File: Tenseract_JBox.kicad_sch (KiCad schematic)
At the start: 14 parts, among them J1 MR30PW-M, J10 Conn_01x04_Pin, J11 Conn_01x04_Pin, J12 Conn_01x04_Pin, J15 TEST_IN, J16 TEST_OUT, J17 DO_SEL, J19 DO_SEL, J2 WS2815_01_IN, J3 WS2815_02_IN, J4 MR30PW-FB, J5 WS2815_01_OUT, J6 WS2815_02_OUT, J8 Conn_01x04_Pin

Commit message: Finished 2nd pcb
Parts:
- added J15: DO_SEL2, Connector_PinHeader_2.54mm:PinHeader_1x03_P2.54mm_Vertical, symbol Connector:Conn_01x03_Pin
- J14: renamed from J17; value DO_SEL -> DO_SEL1
- renumbered J12 to J10, J6 to J11, J11 to J12, J16 to J13, J8 to J3, J3 to J4, J10 to J5, J15 to J6, J19 to J7, J4 to J8, J5 to J9
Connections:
- net BO2: now also J15.3 (Pin_3)
- net DO: now also J15.2 (Pin_2)
- net DO1: now also J14.3 (Pin_3); no longer J14.1 (Pin_1)
- net DO2: now also J15.1 (Pin_1); no longer J14.3 (Pin_3)
- net B01 renamed BO1
- net BO1: now also J14.1 (Pin_1)
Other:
- moved on the sheet: J10, J14

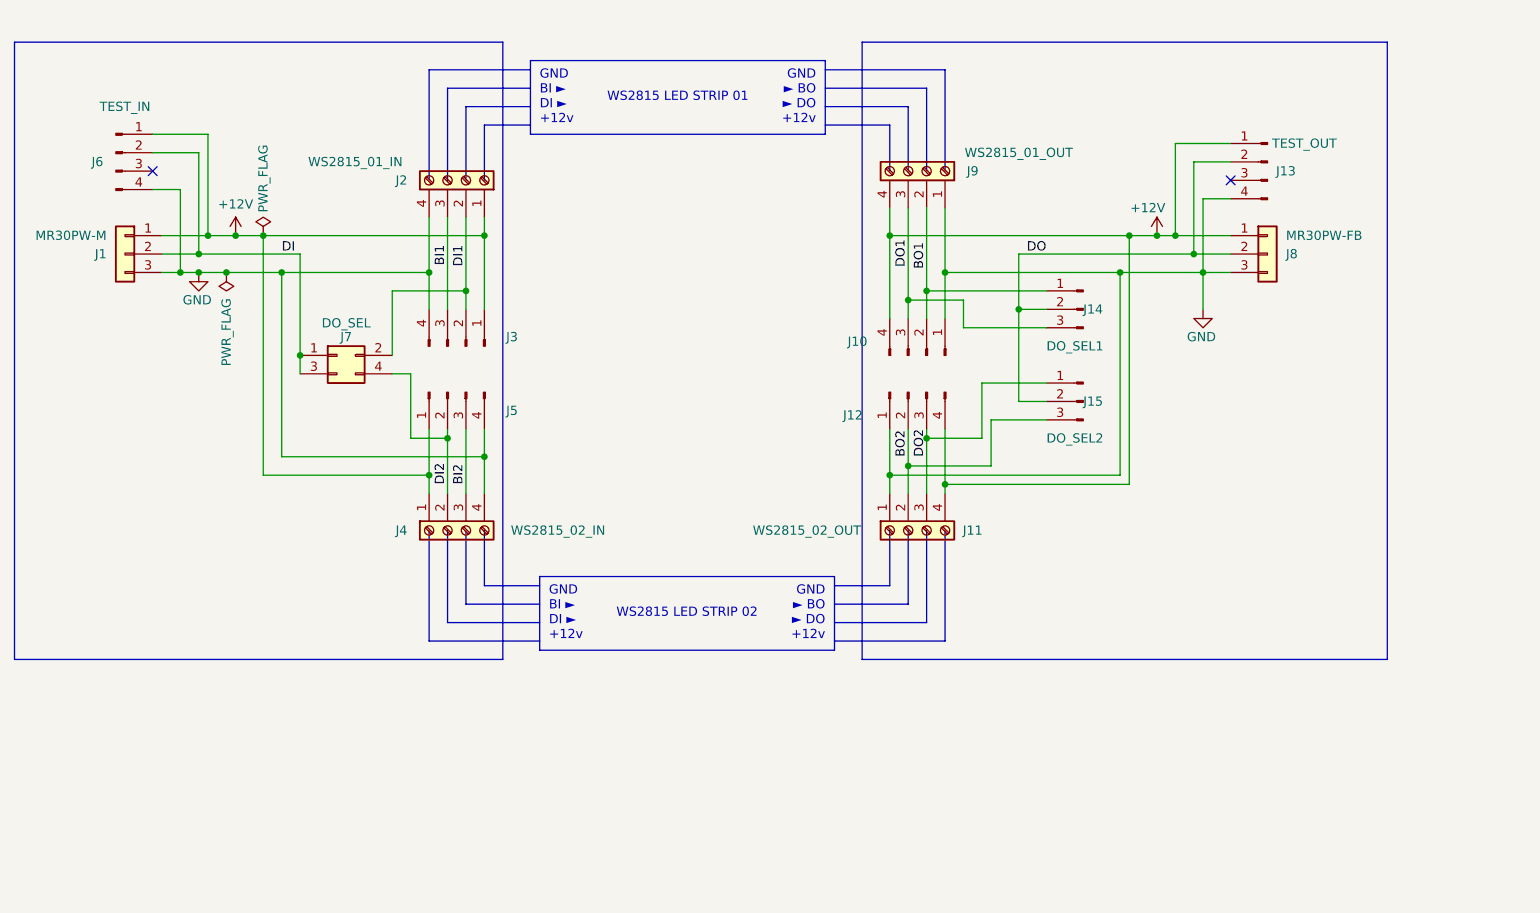
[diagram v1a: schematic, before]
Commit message: Added grouping boxes to schematic
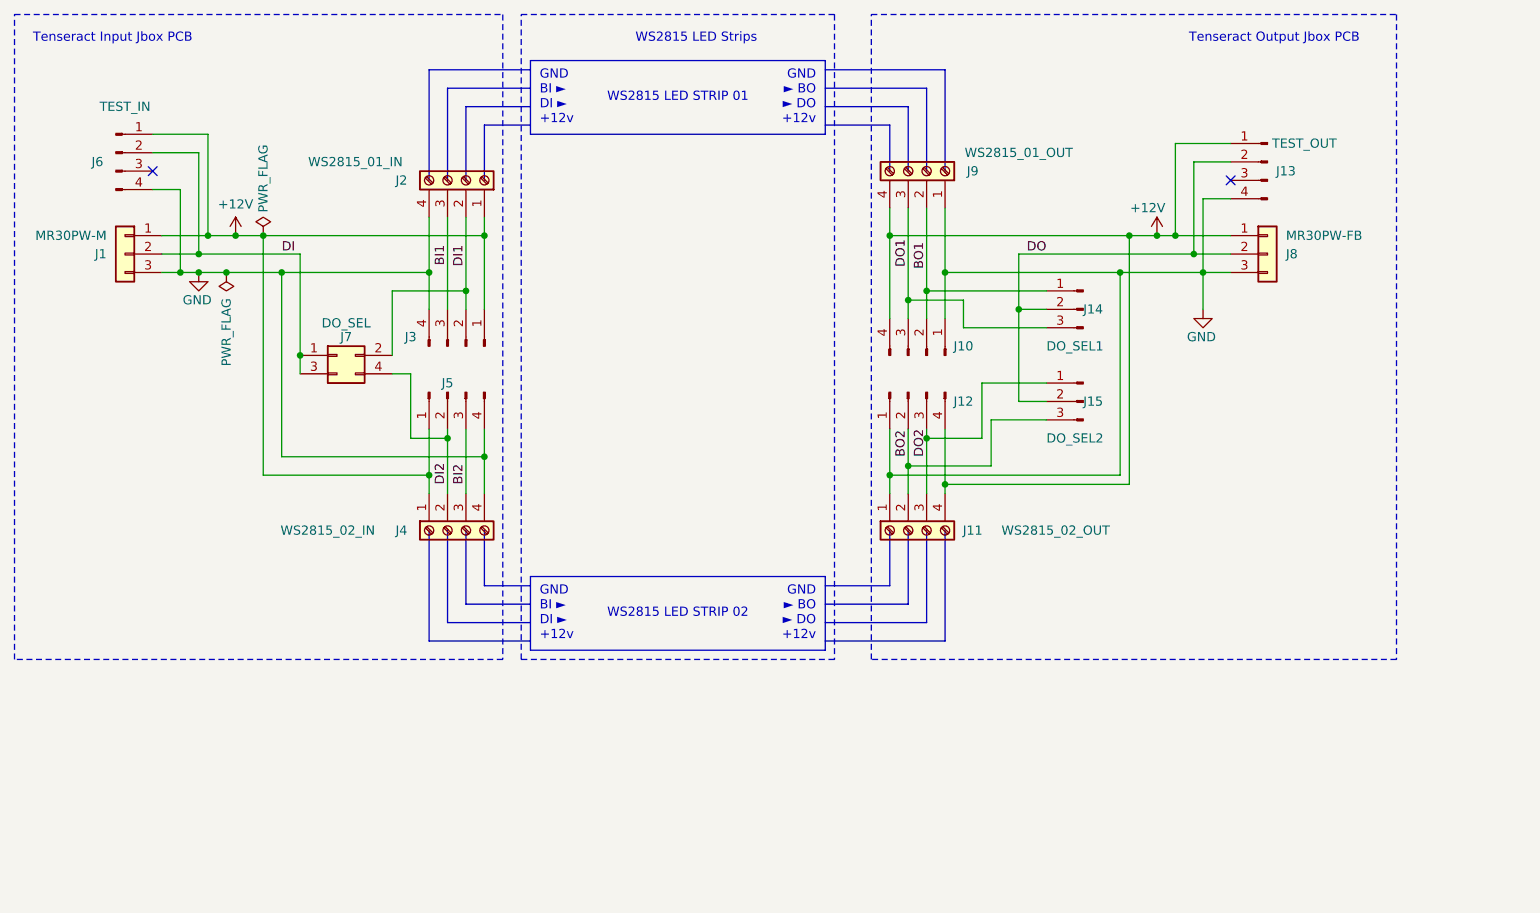
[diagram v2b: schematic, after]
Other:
- note added: "Tenseract Input Jbox PCB"
- note added: "Tenseract Output Jbox PCB"
- note added: "WS2815 LED Strips"
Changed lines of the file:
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@@
 	(paper "A4")
 	(rectangle
-		(start 97.79 99.06)
-		(end 138.43 109.22)
+		(start 96.52 99.06)
+		(end 137.16 109.22)
 		(stroke
 			(width 0)
@@
 	)
 	(rectangle
-		(start 142.24 25.4)
-		(end 214.63 110.49)
-		(stroke
-			(width 0)
-			(type default)
+		(start 143.51 21.59)
+		(end 215.9 110.49)
+		(stroke
+			(width 0)
+			(type dash)
 		)
 		(fill
@@
 	)
 	(rectangle
-		(start 25.4 25.4)
+		(start 95.25 21.59)
+		(end 138.43 110.49)
+		(stroke
+			(width 0)
+			(type dash)
+		)
+		(fill
+			(type none)
+		)
+	)
+	(rectangle
+		(start 25.4 21.59)
 		(end 92.71 110.49)
 		(stroke
 			(width 0)
-			(type default)
+			(type dash)
 		)
 		(fill
@@
 	(text "WS2815 LED STRIP 02"
 		(exclude_from_sim no)
-		(at 118.11 104.14 0)
+		(at 116.84 104.14 0)
 		(effects
 			(font
 				(size 1.27 1.27)
 			)
+		)
+	)
+	(text "Tenseract Input Jbox PCB"
+		(exclude_from_sim no)
+		(at 27.94 24.13 0)
+		(effects
+			(font
+				(size 1.27 1.27)
+			)
+			(justify left top)
 		)
 	)
@@
 		)
 	)
+	(text "Tenseract Output Jbox PCB"
+		(exclude_from_sim no)
+		(at 210.82 24.13 0)
+		(effects
+			(font
+				(size 1.27 1.27)
+			)
+			(justify right top)
+		)
+	)
 	(text "GND\nBI ►\nDI ►\n+12v"
 		(exclude_from_sim no)
-		(at 99.06 104.14 0)
+		(at 97.79 104.14 0)
 		(effects
 			(font
@@
 	(text "GND\n► BO\n► DO\n+12v"
 		(exclude_from_sim no)
-		(at 137.16 104.14 0)
+		(at 135.89 104.14 0)
 		(effects
 			(font
@@
 		)
 	)
+	(text "WS2815 LED Strips"
+		(exclude_from_sim no)
+		(at 119.38 24.13 0)
+		(effects
+			(font
+				(size 1.27 1.27)
+			)
+			(justify top)
+		)
+	)
 	(junction
 		(at 52.07 52.07)
@@
 	(polyline
 		(pts
-			(xy 82.55 107.95) (xy 97.79 107.95)
+			(xy 82.55 107.95) (xy 96.52 107.95)
 		)
 		(stroke
@@
 	(polyline
 		(pts
-			(xy 90.17 100.33) (xy 97.79 100.33)
-		)
-		(stroke
-			(width 0)
-			(type default)
-		)
-	)
-	(polyline
-		(pts
-			(xy 138.43 107.95) (xy 153.67 107.95)
+			(xy 90.17 100.33) (xy 96.52 100.33)
+		)
+		(stroke
+			(width 0)
+			(type default)
+		)
+	)
+	(polyline
+		(pts
+			(xy 137.16 107.95) (xy 153.67 107.95)
 		)
 		(stroke
@@
 	(polyline
 		(pts
-			(xy 138.43 100.33) (xy 146.05 100.33)
+			(xy 137.16 100.33) (xy 146.05 100.33)
 		)
 		(stroke
@@
 	(polyline
 		(pts
-			(xy 138.43 105.41) (xy 151.13 105.41)
+			(xy 137.16 105.41) (xy 151.13 105.41)
 		)
 		(stroke
@@
 	(polyline
 		(pts
-			(xy 138.43 102.87) (xy 148.59 102.87)
+			(xy 137.16 102.87) (xy 148.59 102.87)
 		)
 		(stroke
@@
 	(polyline
 		(pts
-			(xy 87.63 102.87) (xy 97.79 102.87)
+			(xy 87.63 102.87) (xy 96.52 102.87)
 		)
 		(stroke
@@
 	(polyline
 		(pts
-			(xy 85.09 105.41) (xy 97.79 105.41)
+			(xy 85.09 105.41) (xy 96.52 105.41)
 		)
 		(stroke
@@
 		(dnp no)
 		(property "Reference" "J12"
-			(at 140.97 76.835 90)
+			(at 156.21 74.93 90)
 			(show_name no)
 			(do_not_autoplace no)
@@
 		(dnp no)
 		(property "Reference" "J10"
-			(at 141.605 66.675 90)
+			(at 156.21 67.31 90)
 			(show_name no)
 			(do_not_autoplace no)
@@
 		(dnp no)
 		(property "Reference" "J3"
-			(at 93.98 66.04 90)
+			(at 80.01 66.04 90)
 			(show_name no)
 			(do_not_autoplace no)
@@
 		)
 		(property "Value" "WS2815_02_OUT"
-			(at 134.62 92.71 90)
+			(at 168.91 92.71 90)
 			(show_name no)
 			(do_not_autoplace no)
@@
 		(dnp no)
 		(property "Reference" "J5"
-			(at 93.98 76.2 90)
+			(at 85.09 72.39 90)
 			(show_name no)
 			(do_not_autoplace no)
@@
 		)
 		(property "Value" "WS2815_02_IN"
-			(at 100.33 92.71 90)
-			(show_name no)
-			(do_not_autoplace no)
+			(at 68.58 92.71 90)
+			(show_name no)
+			(do_not_autoplace no)

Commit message: Updated schematic formating, set revsion to 1.0
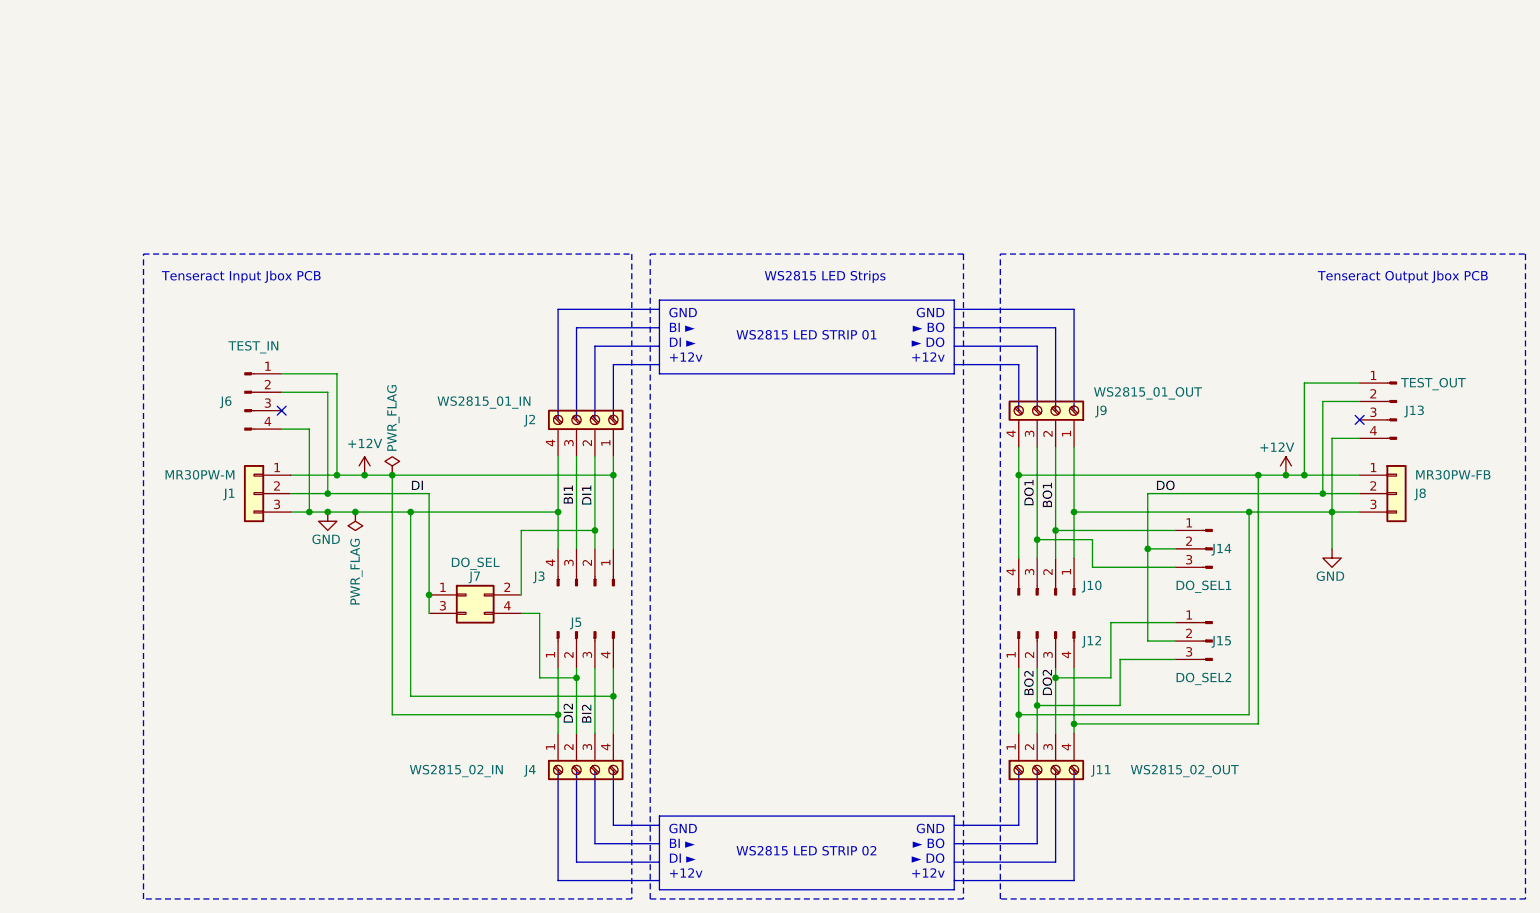
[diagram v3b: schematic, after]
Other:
- title: (none) -> Tenseract
- moved on the sheet: J1, J10, J11, J12, J13, J14, J15, J2, J3, J4, J5, J6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
